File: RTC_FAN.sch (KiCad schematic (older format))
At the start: 0 parts

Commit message: Drawn schematic of RTC
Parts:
- added C?: C_Small, Capacitor_SMD:C_0603_1608Metric_Pad1.08x0.95mm_HandSolder, symbol Device:C_Small
- added C?: 0.1uF, Capacitor_SMD:C_0603_1608Metric_Pad1.08x0.95mm_HandSolder, symbol Device:C_Small
- added R?: R_Small_US, Resistor_SMD:R_0603_1608Metric_Pad0.98x0.95mm_HandSolder, symbol Device:R_Small_US
- added R? (x4): 1K, Resistor_SMD:R_0603_1608Metric_Pad0.98x0.95mm_HandSolder, symbol Device:R_Small_US
- added U?: DS3231S#, SOIC127P1032X265-16N, symbol GM_Clock_n_Timers:DS3231S#
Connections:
- net labels added: GNDD, RTC_OSC_OUT, RTC_RST, RTC_SCL, RTC_SDA, RTC_SQW, VCC3V3
- wire segments 0 -> 55
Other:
- note added: "tR = 300 : 1000 nS\ncB = 400 pF\n\nR = tR/cB"

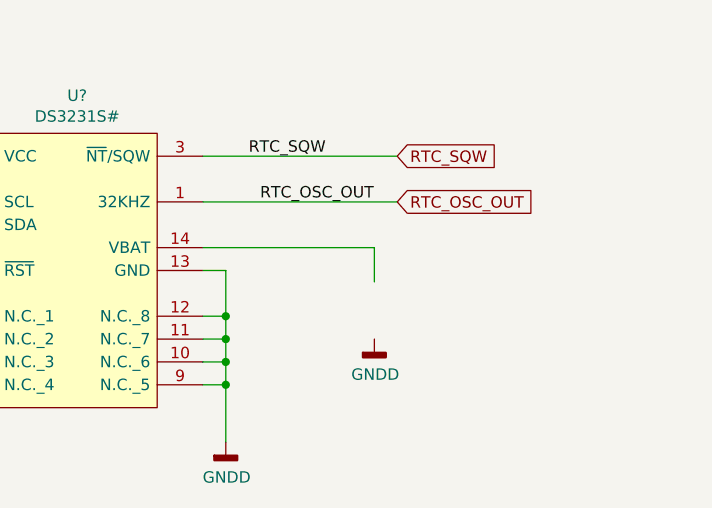
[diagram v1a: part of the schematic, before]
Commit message: Added battery holder to the RTC clock
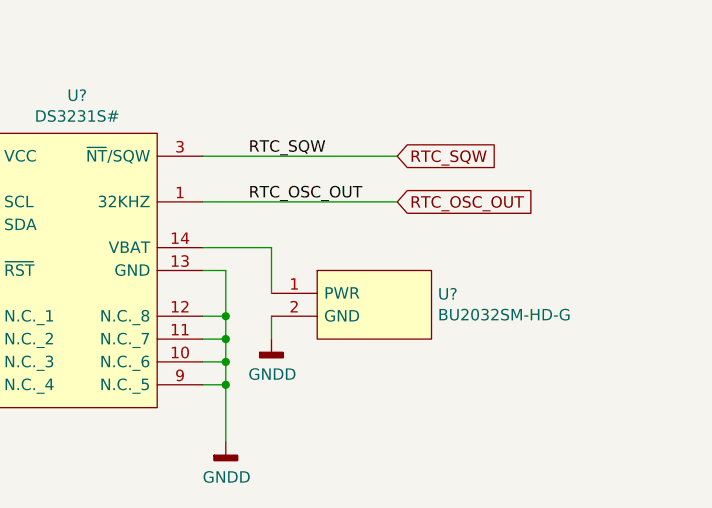
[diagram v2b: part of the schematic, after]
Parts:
- added U?: BU2032SM-HD-G, BU2032SM-HD-G, symbol GM_Battery_Holders_n_Contacts:BU2032SM-HD-G
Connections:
- wire segments 55 -> 56
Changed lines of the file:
@@
 Text Label 2500 3600 0    50   ~ 0
 RTC_RST
-Wire Wire Line
-	4300 3500 5050 3500
-Wire Wire Line
-	5050 3500 5050 3650
 Text Label 4500 3100 0    50   ~ 0
 RTC_SQW
-Text Label 4550 3300 0    50   ~ 0
+Text Label 4500 3300 0    50   ~ 0
 RTC_OSC_OUT
 Text GLabel 2250 3300 0    50   Input ~ 0
@@
 L power:GNDD #PWR?
 U 1 1 6025F3F3
-P 5050 3900
+P 4600 3900
 AR Path="/601DF0A6/6025F3F3" Ref="#PWR?"  Part="1"
 AR Path="/601E7C5A/6025F3F3" Ref="#PWR?"  Part="1"
 AR Path="/601E7CC8/6025F3F3" Ref="#PWR?"  Part="1"
-F 0 "#PWR?" H 5050 3650 50  0001 C CNN
-F 1 "GNDD" H 5054 3745 50  0000 C CNN
-F 2 "" H 5050 3900 50  0001 C CNN
-F 3 "" H 5050 3900 50  0001 C CNN
-	1    5050 3900
+F 0 "#PWR?" H 4600 3650 50  0001 C CNN
+F 1 "GNDD" H 4604 3745 50  0000 C CNN
+F 2 "" H 4600 3900 50  0001 C CNN
+F 3 "" H 4600 3900 50  0001 C CNN
+	1    4600 3900
 	1    0    0    -1
 $EndComp
+$Comp
+L GM_Battery_Holders_n_Contacts:BU2032SM-HD-G U?
+U 1 1 6022F346
+P 4800 3600
+F 0 "U?" H 5328 3496 50  0000 L CNN
+F 1 "BU2032SM-HD-G" H 5328 3405 50  0000 L CNN
+F 2 "BU2032SM-HD-G" H 5450 3700 50  0001 L CNN
+F 3 "http://www.memoryprotectiondevices.com/datasheets/BU2032SM-HD-G-datasheet.pdf" H 5450 3600 50  0001 L CNN
+F 4 "BU2032SM-HD-G" H 5800 3600 50  0001 C CNN "MPN"
+	1    4800 3600
+	1    0    0    -1
+$EndComp
+Wire Wire Line
+	4600 3500 4600 3700
+Wire Wire Line
+	4600 3800 4600 3900
+Wire Wire Line
+	4600 3500 4300 3500
 $EndSCHEMATC
